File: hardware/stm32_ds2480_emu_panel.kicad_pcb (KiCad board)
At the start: 2 copper layers, 70 x 84 mm, 288 parts, among them J1 OW, J2 USB_A, J3 SWD, Q1 SI2302CDS, U1 USBLC6-2SC6, U2 STM32F042F6Px, U3 AP2204K-3.3

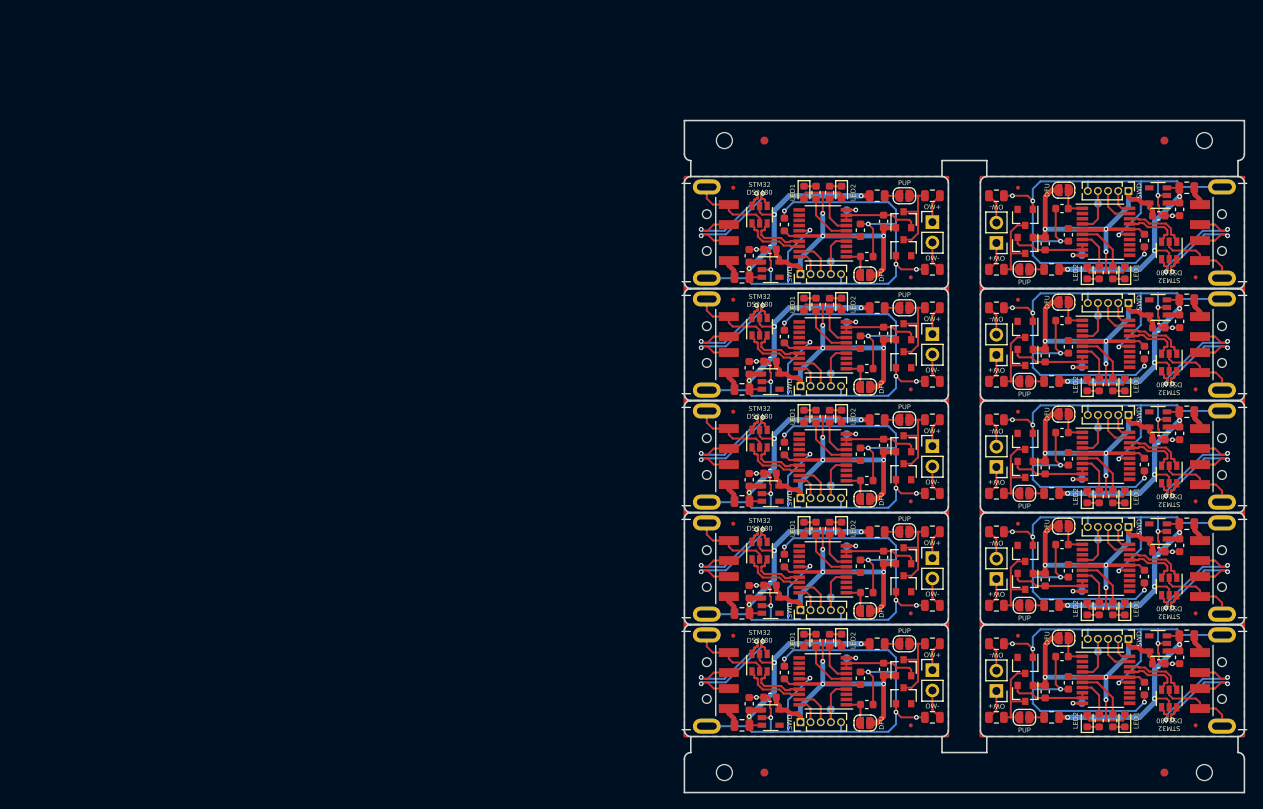
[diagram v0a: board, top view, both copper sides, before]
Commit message: Started using KiKit for the panelization.
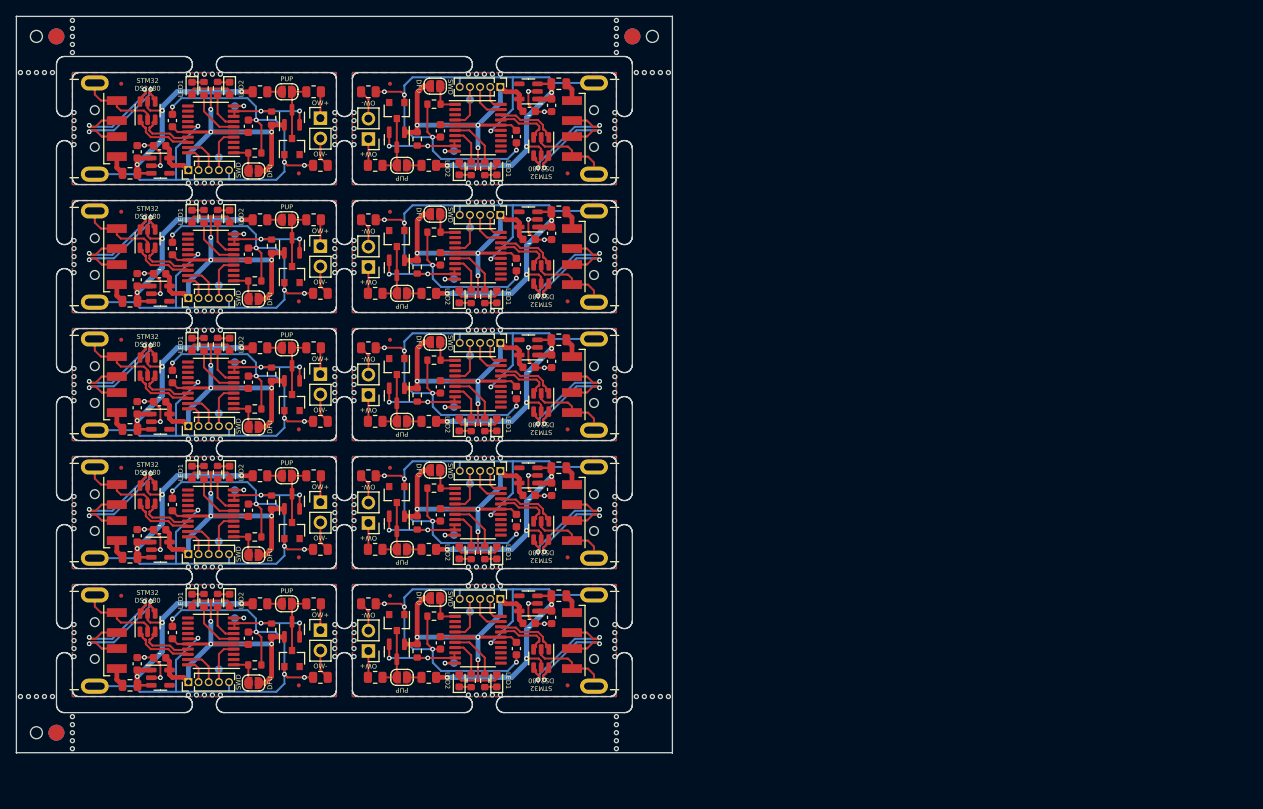
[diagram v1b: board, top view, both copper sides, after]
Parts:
- removed the C1 at (167.5, 120.0)
- removed the C1 at (122.5, 62.0)
- removed the C1 at (167.5, 106.0)
- removed the C1 at (167.5, 92.0)
- removed the C1 at (167.5, 78.0)
- removed the C1 at (122.5, 118.0)
- removed the C1 at (122.5, 104.0)
- removed the C1 at (122.5, 90.0)
- removed the C1 at (122.5, 76.0)
- removed the C1 at (167.5, 64.0)
- removed the C2 at (158.0, 119.3)
- removed the C2 at (132.0, 62.7)
- removed the C2 at (158.0, 105.3)
- removed the C2 at (158.0, 91.3)
- removed the C2 at (158.0, 77.3)
- removed the C2 at (132.0, 118.7)
- removed the C2 at (132.0, 104.7)
- removed the C2 at (132.0, 90.7)
- removed the C2 at (132.0, 76.7)
- removed the C2 at (158.0, 63.3)
- removed the C3 at (169.3, 116.9)
- removed the C3 at (120.7, 65.1)
- removed the C3 at (169.3, 102.9)
- removed the C3 at (169.3, 88.9)
- removed the C3 at (169.3, 74.9)
- removed the C3 at (120.7, 121.1)
- removed the C3 at (120.7, 107.1)
- removed the C3 at (120.7, 93.1)
- removed the C3 at (120.7, 79.1)
- removed the C3 at (169.3, 60.9)
- removed the C4 at (171.9, 116.1)
- removed the C4 at (118.1, 65.9)
- removed the C4 at (171.9, 102.1)
- removed the C4 at (171.9, 88.1)
- removed the C4 at (171.9, 74.1)
- removed the C4 at (118.1, 121.9)
- removed the C4 at (118.1, 107.9)
- removed the C4 at (118.1, 93.9)
- removed the C4 at (118.1, 79.9)
- removed the C4 at (171.9, 60.1)
- removed the D1 at (125.0, 114.0)
- removed the D1 at (125.0, 58.0)
- removed the D1 at (125.0, 100.0)
- removed the D1 at (125.0, 86.0)
- removed the D1 at (125.0, 72.0)
- removed the D1 at (165.1, 124.0)
- removed the D1 at (165.1, 110.0)
- removed the D1 at (165.1, 96.0)
- removed the D1 at (165.1, 82.0)
- removed the D1 at (165.1, 68.0)
- removed the D2 at (160.3, 124.0)
- removed the D2 at (129.7, 58.0)
- removed the D2 at (160.3, 110.0)
- removed the D2 at (160.3, 96.0)
- removed the D2 at (160.3, 82.0)
- removed the D2 at (129.7, 114.0)
- removed the D2 at (129.7, 100.0)
- removed the D2 at (129.7, 86.0)
- removed the D2 at (129.7, 72.0)
- removed the D2 at (160.3, 68.0)
- removed the D3 at (152.6, 117.1)
- removed the D3 at (137.4, 64.9)
- removed the D3 at (152.6, 103.1)
- removed the D3 at (152.6, 89.1)
- removed the D3 at (152.6, 75.1)
- removed the D3 at (137.4, 120.9)
- removed the D3 at (137.4, 106.9)
- removed the D3 at (137.4, 92.9)
- removed the D3 at (137.4, 78.9)
- removed the D3 at (152.6, 61.1)
- removed the F1 at (117.2, 124.6)
- removed the F1 at (117.2, 68.6)
- removed the F1 at (117.2, 110.6)
- removed the F1 at (117.2, 96.6)
- removed the F1 at (117.2, 82.6)
- removed the F1 at (172.8, 113.4)
- removed the F1 at (172.8, 99.4)
- removed the F1 at (172.8, 85.4)
- removed the F1 at (172.8, 71.4)
- removed the F1 at (172.8, 57.4)
- removed the FID1 at (173.9, 124.6)
- removed the FID1 at (116.1, 57.4)
- removed the FID1 at (173.9, 110.6)
- removed the FID1 at (173.9, 96.6)
- removed the FID1 at (173.9, 82.6)
- removed the FID1 at (116.1, 113.4)
- removed the FID1 at (116.1, 99.4)
- removed the FID1 at (116.1, 85.4)
- removed the FID1 at (116.1, 71.4)
- removed the FID1 at (173.9, 68.6)
- removed the FID2 at (138.3, 124.6)
- removed the FID2 at (138.3, 68.6)
- removed the FID2 at (138.3, 110.6)
- removed the FID2 at (138.3, 96.6)
- removed the FID2 at (138.3, 82.6)
- removed the FID2 at (151.7, 113.4)
- removed the FID2 at (151.7, 99.4)
- removed the FID2 at (151.7, 85.4)
- removed the FID2 at (151.7, 71.4)
- removed the FID2 at (151.7, 57.4)
- removed FID_A1 (x2), FID_A2 (x2): Fiducial_1mm_Mask2mm, Fiducial:Fiducial_1mm_Mask2mm
- removed the J1 at (141.0, 117.7)
- removed the J1 at (141.0, 61.7)
- removed the J1 at (141.0, 103.7)
- removed the J1 at (141.0, 89.7)
- removed the J1 at (141.0, 75.7)
- removed the J1 at (149.0, 120.3)
- removed the J1 at (149.0, 106.3)
- removed the J1 at (149.0, 92.3)
- removed the J1 at (149.0, 78.3)
- removed the J1 at (149.0, 64.3)
- removed the J2 at (105.9, 119.0)
- removed the J2 at (105.9, 63.0)
- removed the J2 at (105.9, 105.0)
- removed the J2 at (105.9, 91.0)
- removed the J2 at (105.9, 77.0)
- removed the J2 at (184.1, 119.0)
- removed the J2 at (184.1, 105.0)
- removed the J2 at (184.1, 91.0)
- removed the J2 at (184.1, 77.0)
- removed the J2 at (184.1, 63.0)
- removed the J3 at (165.5, 113.8)
- removed the J3 at (124.5, 68.2)
- removed the J3 at (165.5, 99.8)
- removed the J3 at (165.5, 85.8)
- removed the J3 at (165.5, 71.8)
- removed the J3 at (124.5, 124.2)
- removed the J3 at (124.5, 110.2)
- removed the J3 at (124.5, 96.2)
- removed the J3 at (124.5, 82.2)
- removed the J3 at (165.5, 57.8)
- removed the JP1 at (152.5, 123.6)
- removed the JP1 at (137.5, 58.4)
- removed the JP1 at (152.5, 109.6)
- removed the JP1 at (152.5, 95.6)
- removed the JP1 at (152.5, 81.6)
- removed the JP1 at (137.5, 114.4)
- removed the JP1 at (137.5, 100.4)
- removed the JP1 at (137.5, 86.4)
- removed the JP1 at (137.5, 72.4)
- removed the JP1 at (152.5, 67.6)
- removed the JP2 at (132.6, 124.3)
- removed the JP2 at (132.6, 68.3)
- removed the JP2 at (132.6, 110.3)
- removed the JP2 at (132.6, 96.3)
- removed the JP2 at (132.6, 82.3)
- removed the JP2 at (157.4, 113.7)
- removed the JP2 at (157.4, 99.7)
- removed the JP2 at (157.4, 85.7)
- removed the JP2 at (157.4, 71.7)
- removed the JP2 at (157.4, 57.7)
- removed the Q1 at (152.6, 120.6)
- removed the Q1 at (137.4, 61.4)
- removed the Q1 at (152.6, 106.6)
- removed the Q1 at (152.6, 92.6)
- removed the Q1 at (152.6, 78.6)
- removed the Q1 at (137.4, 117.4)
- removed the Q1 at (137.4, 103.4)
- removed the Q1 at (137.4, 89.4)
- removed the Q1 at (137.4, 75.4)
- removed the Q1 at (152.6, 64.6)
- removed the R1 at (163.6, 124.0)
- removed the R1 at (126.5, 58.0)
- removed the R1 at (163.6, 110.0)
- removed the R1 at (163.6, 96.0)
- removed the R1 at (163.6, 82.0)
- removed the R1 at (126.5, 114.0)
- removed the R1 at (126.5, 100.0)
- removed the R1 at (126.5, 86.0)
- removed the R1 at (126.5, 72.0)
- removed the R1 at (163.6, 68.0)
- removed the R2 at (161.8, 124.0)
- removed the R2 at (128.2, 58.0)
- removed the R2 at (161.8, 110.0)
- removed the R2 at (161.8, 96.0)
- removed the R2 at (161.8, 82.0)
- removed the R2 at (128.2, 114.0)
- removed the R2 at (128.2, 100.0)
- removed the R2 at (128.2, 86.0)
- removed the R2 at (128.2, 72.0)
- removed the R2 at (161.8, 68.0)
- removed the R3 at (134.1, 114.4)
- removed the R3 at (134.1, 58.4)
- removed the R3 at (134.1, 100.4)
- removed the R3 at (134.1, 86.4)
- removed the R3 at (134.1, 72.4)
- removed the R3 at (155.9, 123.6)
- removed the R3 at (155.9, 109.6)
- removed the R3 at (155.9, 95.6)
- removed the R3 at (155.9, 81.6)
- removed the R3 at (155.9, 67.6)
- removed the R4 at (141.0, 114.4)
- removed the R4 at (141.0, 58.4)
- removed the R4 at (141.0, 100.4)
- removed the R4 at (141.0, 86.4)
- removed the R4 at (141.0, 72.4)
- removed the R4 at (149.0, 123.6)
- removed the R4 at (149.0, 109.6)
- removed the R4 at (149.0, 95.6)
- removed the R4 at (149.0, 81.6)
- removed the R4 at (149.0, 67.6)
- removed the R5 at (155.1, 120.4)
- removed the R5 at (134.9, 61.6)
- removed the R5 at (155.1, 106.4)
- removed the R5 at (155.1, 92.4)
- removed the R5 at (155.1, 78.4)
- removed the R5 at (134.9, 117.6)
- removed the R5 at (134.9, 103.6)
- removed the R5 at (134.9, 89.6)
- removed the R5 at (134.9, 75.6)
- removed the R5 at (155.1, 64.4)
- removed the R6 at (157.2, 116.0)
- removed the R6 at (132.8, 66.0)
- removed the R6 at (157.2, 102.0)
- removed the R6 at (157.2, 88.0)
- removed the R6 at (157.2, 74.0)
- removed the R6 at (132.8, 122.0)
- removed the R6 at (132.8, 108.0)
- removed the R6 at (132.8, 94.0)
- removed the R6 at (132.8, 80.0)
- removed the R6 at (157.2, 60.0)
- removed the R7 at (149.0, 114.4)
- removed the R7 at (141.0, 67.6)
- removed the R7 at (149.0, 100.4)
- removed the R7 at (149.0, 86.4)
- removed the R7 at (149.0, 72.4)
- removed the R7 at (141.0, 123.6)
- removed the R7 at (141.0, 109.6)
- removed the R7 at (141.0, 95.6)
- removed the R7 at (141.0, 81.6)
- removed the R7 at (149.0, 58.4)
- removed the REF** at (115.0, 130.5)
- removed the REF** at (175.0, 130.5)
- removed the REF** at (115.0, 51.5)
- removed the REF** at (175.0, 51.5)
- removed the TP1 at (159.7, 121.8)
- removed the TP1 at (130.3, 60.2)
- removed the TP1 at (159.7, 107.8)
- removed the TP1 at (159.7, 93.8)
- removed the TP1 at (159.7, 79.8)
- removed the TP1 at (130.3, 116.2)
- removed the TP1 at (130.3, 102.2)
- removed the TP1 at (130.3, 88.2)
- removed the TP1 at (130.3, 74.2)
- removed the TP1 at (159.7, 65.8)
- removed the TP2 at (161.7, 115.4)
- removed the TP2 at (128.3, 66.6)
- removed the TP2 at (161.7, 101.4)
- removed the TP2 at (161.7, 87.4)
- removed the TP2 at (161.7, 73.4)
- removed the TP2 at (128.3, 122.6)
- removed the TP2 at (128.3, 108.6)
- removed the TP2 at (128.3, 94.6)
- removed the TP2 at (128.3, 80.6)
- removed the TP2 at (161.7, 59.4)
- removed the U1 at (170.6, 121.2)
- removed the U1 at (119.4, 60.8)
- removed the U1 at (170.6, 107.2)
- removed the U1 at (170.6, 93.2)
- removed the U1 at (170.6, 79.2)
- removed the U1 at (119.4, 116.8)
- removed the U1 at (119.4, 102.8)
- removed the U1 at (119.4, 88.8)
- removed the U1 at (119.4, 74.8)
- removed the U1 at (170.6, 65.2)
- removed the U2 at (162.7, 118.9)
- removed the U2 at (127.3, 63.1)
- removed the U2 at (162.7, 104.9)
- removed the U2 at (162.7, 90.9)
- removed the U2 at (162.7, 76.9)
- removed the U2 at (127.3, 119.1)
- removed the U2 at (127.3, 105.1)
- removed the U2 at (127.3, 91.1)
- removed the U2 at (127.3, 77.1)
- removed the U2 at (162.7, 62.9)
- removed the U3 at (169.2, 114.4)
- removed the U3 at (120.8, 67.6)
- removed the U3 at (169.2, 100.4)
- removed the U3 at (169.2, 86.4)
- removed the U3 at (169.2, 72.4)
- removed the U3 at (120.8, 123.6)
- removed the U3 at (120.8, 109.6)
- removed the U3 at (120.8, 95.6)
- removed the U3 at (120.8, 81.6)
- removed the U3 at (169.2, 58.4)
- added C1: 100nF, Capacitor_SMD:C_0603_1608Metric, F.Cu at (89.0, 99.0)
- added C1: 100nF, Capacitor_SMD:C_0603_1608Metric, F.Cu at (46.0, 65.0)
- added C1: 100nF, Capacitor_SMD:C_0603_1608Metric, F.Cu at (89.0, 67.0)
- added C1: 100nF, Capacitor_SMD:C_0603_1608Metric, F.Cu at (46.0, 97.0)
- added C1: 100nF, Capacitor_SMD:C_0603_1608Metric, F.Cu at (46.0, 81.0)
- added C1: 100nF, Capacitor_SMD:C_0603_1608Metric, F.Cu at (89.0, 51.0)
- added C1: 100nF, Capacitor_SMD:C_0603_1608Metric, F.Cu at (46.0, 49.0)
- added C1: 100nF, Capacitor_SMD:C_0603_1608Metric, F.Cu at (46.0, 113.0)
- added C1: 100nF, Capacitor_SMD:C_0603_1608Metric, F.Cu at (89.0, 83.0)
- added C1: 100nF, Capacitor_SMD:C_0603_1608Metric, F.Cu at (89.0, 115.0)
- added C2: 100nF, Capacitor_SMD:C_0603_1608Metric, F.Cu at (55.5, 81.7)
- added C2: 100nF, Capacitor_SMD:C_0603_1608Metric, F.Cu at (55.5, 113.7)
- added C2: 100nF, Capacitor_SMD:C_0603_1608Metric, F.Cu at (55.5, 65.7)
- added C2: 100nF, Capacitor_SMD:C_0603_1608Metric, F.Cu at (79.5, 114.3)
- added C2: 100nF, Capacitor_SMD:C_0603_1608Metric, F.Cu at (79.5, 98.3)
- added C2: 100nF, Capacitor_SMD:C_0603_1608Metric, F.Cu at (79.5, 82.3)
- added C2: 100nF, Capacitor_SMD:C_0603_1608Metric, F.Cu at (55.5, 97.7)
- added C2: 100nF, Capacitor_SMD:C_0603_1608Metric, F.Cu at (79.5, 50.3)
- added C2: 100nF, Capacitor_SMD:C_0603_1608Metric, F.Cu at (79.5, 66.3)
- added C2: 100nF, Capacitor_SMD:C_0603_1608Metric, F.Cu at (55.5, 49.7)
- added C3: 2.2uF, Capacitor_SMD:C_0603_1608Metric, F.Cu at (90.6, 79.9)
- added C3: 2.2uF, Capacitor_SMD:C_0603_1608Metric, F.Cu at (44.4, 52.1)
- added C3: 2.2uF, Capacitor_SMD:C_0603_1608Metric, F.Cu at (44.4, 116.2)
- added C3: 2.2uF, Capacitor_SMD:C_0603_1608Metric, F.Cu at (44.4, 68.2)
- added C3: 2.2uF, Capacitor_SMD:C_0603_1608Metric, F.Cu at (90.6, 63.9)
- added C3: 2.2uF, Capacitor_SMD:C_0603_1608Metric, F.Cu at (90.6, 47.9)
- added C3: 2.2uF, Capacitor_SMD:C_0603_1608Metric, F.Cu at (44.4, 100.2)
- added C3: 2.2uF, Capacitor_SMD:C_0603_1608Metric, F.Cu at (90.6, 95.9)
- added C3: 2.2uF, Capacitor_SMD:C_0603_1608Metric, F.Cu at (44.4, 84.2)
- added C3: 2.2uF, Capacitor_SMD:C_0603_1608Metric, F.Cu at (90.6, 111.9)
- added C4: 1uF, Capacitor_SMD:C_0603_1608Metric, F.Cu at (41.6, 116.9)
- added C4: 1uF, Capacitor_SMD:C_0603_1608Metric, F.Cu at (41.6, 52.9)
- added C4: 1uF, Capacitor_SMD:C_0603_1608Metric, F.Cu at (93.4, 95.1)
- added C4: 1uF, Capacitor_SMD:C_0603_1608Metric, F.Cu at (93.4, 63.1)
- added C4: 1uF, Capacitor_SMD:C_0603_1608Metric, F.Cu at (93.4, 47.1)
- added C4: 1uF, Capacitor_SMD:C_0603_1608Metric, F.Cu at (41.6, 100.9)
- added C4: 1uF, Capacitor_SMD:C_0603_1608Metric, F.Cu at (41.6, 68.9)
- added C4: 1uF, Capacitor_SMD:C_0603_1608Metric, F.Cu at (41.6, 84.9)
- added C4: 1uF, Capacitor_SMD:C_0603_1608Metric, F.Cu at (93.4, 111.1)
- added C4: 1uF, Capacitor_SMD:C_0603_1608Metric, F.Cu at (93.4, 79.1)
- added D1: LED1, LED_SMD:LED_0603_1608Metric, F.Cu at (86.6, 119.0)
- added D1: LED1, LED_SMD:LED_0603_1608Metric, F.Cu at (48.4, 93.0)
- added D1: LED1, LED_SMD:LED_0603_1608Metric, F.Cu at (86.6, 71.0)
- added D1: LED1, LED_SMD:LED_0603_1608Metric, F.Cu at (48.4, 77.0)
- added D1: LED1, LED_SMD:LED_0603_1608Metric, F.Cu at (86.6, 87.0)
- added D1: LED1, LED_SMD:LED_0603_1608Metric, F.Cu at (48.4, 45.0)
- added D1: LED1, LED_SMD:LED_0603_1608Metric, F.Cu at (48.4, 61.0)
- added D1: LED1, LED_SMD:LED_0603_1608Metric, F.Cu at (86.6, 103.0)
- added D1: LED1, LED_SMD:LED_0603_1608Metric, F.Cu at (48.4, 109.0)
- added D1: LED1, LED_SMD:LED_0603_1608Metric, F.Cu at (86.6, 55.0)
- added D2: LED2, LED_SMD:LED_0603_1608Metric, F.Cu at (81.9, 103.0)
- added D2: LED2, LED_SMD:LED_0603_1608Metric, F.Cu at (81.9, 87.0)
- added D2: LED2, LED_SMD:LED_0603_1608Metric, F.Cu at (53.1, 61.0)
- added D2: LED2, LED_SMD:LED_0603_1608Metric, F.Cu at (81.9, 119.0)
- added D2: LED2, LED_SMD:LED_0603_1608Metric, F.Cu at (53.1, 77.0)
- added D2: LED2, LED_SMD:LED_0603_1608Metric, F.Cu at (81.9, 55.0)
- added D2: LED2, LED_SMD:LED_0603_1608Metric, F.Cu at (53.1, 109.0)
- added D2: LED2, LED_SMD:LED_0603_1608Metric, F.Cu at (53.1, 93.0)
- added D2: LED2, LED_SMD:LED_0603_1608Metric, F.Cu at (53.1, 45.0)
- added D2: LED2, LED_SMD:LED_0603_1608Metric, F.Cu at (81.9, 71.0)
- added D3: 5.1V, Diode_SMD:D_SOT-23_ANK, F.Cu at (60.9, 84.3)
- added D3: 5.1V, Diode_SMD:D_SOT-23_ANK, F.Cu at (74.1, 95.8)
- added D3: 5.1V, Diode_SMD:D_SOT-23_ANK, F.Cu at (74.1, 63.8)
- added D3: 5.1V, Diode_SMD:D_SOT-23_ANK, F.Cu at (60.9, 68.3)
- added D3: 5.1V, Diode_SMD:D_SOT-23_ANK, F.Cu at (74.1, 79.8)
- added D3: 5.1V, Diode_SMD:D_SOT-23_ANK, F.Cu at (74.1, 47.8)
- added D3: 5.1V, Diode_SMD:D_SOT-23_ANK, F.Cu at (60.9, 52.2)
- added D3: 5.1V, Diode_SMD:D_SOT-23_ANK, F.Cu at (74.1, 111.8)
- added D3: 5.1V, Diode_SMD:D_SOT-23_ANK, F.Cu at (60.9, 100.3)
- added D3: 5.1V, Diode_SMD:D_SOT-23_ANK, F.Cu at (60.9, 116.3)
- added F1: Polyfuse, Fuse:Fuse_0805_2012Metric, F.Cu at (94.3, 60.4)
- added F1: Polyfuse, Fuse:Fuse_0805_2012Metric, F.Cu at (40.7, 55.6)
- added F1: Polyfuse, Fuse:Fuse_0805_2012Metric, F.Cu at (94.3, 92.4)
- added F1: Polyfuse, Fuse:Fuse_0805_2012Metric, F.Cu at (40.7, 87.6)
- added F1: Polyfuse, Fuse:Fuse_0805_2012Metric, F.Cu at (40.7, 103.6)
- added F1: Polyfuse, Fuse:Fuse_0805_2012Metric, F.Cu at (94.3, 108.4)
- added F1: Polyfuse, Fuse:Fuse_0805_2012Metric, F.Cu at (94.3, 44.4)
- added F1: Polyfuse, Fuse:Fuse_0805_2012Metric, F.Cu at (94.3, 76.4)
- added F1: Polyfuse, Fuse:Fuse_0805_2012Metric, F.Cu at (40.7, 119.6)
- added F1: Polyfuse, Fuse:Fuse_0805_2012Metric, F.Cu at (40.7, 71.6)
- added FID1: Fiducial, Fiducial:Fiducial_0.5mm_Mask1.5mm, F.Cu at (39.6, 108.4)
- added FID1: Fiducial, Fiducial:Fiducial_0.5mm_Mask1.5mm, F.Cu at (39.6, 60.4)
- added FID1: Fiducial, Fiducial:Fiducial_0.5mm_Mask1.5mm, F.Cu at (95.4, 103.6)
- added FID1: Fiducial, Fiducial:Fiducial_0.5mm_Mask1.5mm, F.Cu at (39.6, 92.4)
- added FID1: Fiducial, Fiducial:Fiducial_0.5mm_Mask1.5mm, F.Cu at (39.6, 44.4)
- added FID1: Fiducial, Fiducial:Fiducial_0.5mm_Mask1.5mm, F.Cu at (39.6, 76.4)
- added FID1: Fiducial, Fiducial:Fiducial_0.5mm_Mask1.5mm, F.Cu at (95.4, 71.6)
- added FID1: Fiducial, Fiducial:Fiducial_0.5mm_Mask1.5mm, F.Cu at (95.4, 55.6)
- added FID1: Fiducial, Fiducial:Fiducial_0.5mm_Mask1.5mm, F.Cu at (95.4, 87.6)
- added FID1: Fiducial, Fiducial:Fiducial_0.5mm_Mask1.5mm, F.Cu at (95.4, 119.6)
- added FID2: Fiducial, Fiducial:Fiducial_0.5mm_Mask1.5mm, F.Cu at (73.2, 44.4)
- added FID2: Fiducial, Fiducial:Fiducial_0.5mm_Mask1.5mm, F.Cu at (73.2, 60.4)
- added FID2: Fiducial, Fiducial:Fiducial_0.5mm_Mask1.5mm, F.Cu at (73.2, 92.4)
- added FID2: Fiducial, Fiducial:Fiducial_0.5mm_Mask1.5mm, F.Cu at (61.8, 55.6)
- added FID2: Fiducial, Fiducial:Fiducial_0.5mm_Mask1.5mm, F.Cu at (61.8, 103.6)
- added FID2: Fiducial, Fiducial:Fiducial_0.5mm_Mask1.5mm, F.Cu at (61.8, 87.6)
- added FID2: Fiducial, Fiducial:Fiducial_0.5mm_Mask1.5mm, F.Cu at (61.8, 119.6)
- added FID2: Fiducial, Fiducial:Fiducial_0.5mm_Mask1.5mm, F.Cu at (73.2, 108.4)
- added FID2: Fiducial, Fiducial:Fiducial_0.5mm_Mask1.5mm, F.Cu at (73.2, 76.4)
- added FID2: Fiducial, Fiducial:Fiducial_0.5mm_Mask1.5mm, F.Cu at (61.8, 71.6)
- added J1: OW, Connector_PinHeader_2.54mm:PinHeader_1x02_P2.54mm_Vertical, F.Cu at (70.5, 83.3)
- added J1: OW, Connector_PinHeader_2.54mm:PinHeader_1x02_P2.54mm_Vertical, F.Cu at (64.5, 48.7)
- added J1: OW, Connector_PinHeader_2.54mm:PinHeader_1x02_P2.54mm_Vertical, F.Cu at (64.5, 112.7)
- added J1: OW, Connector_PinHeader_2.54mm:PinHeader_1x02_P2.54mm_Vertical, F.Cu at (70.5, 115.3)
- added J1: OW, Connector_PinHeader_2.54mm:PinHeader_1x02_P2.54mm_Vertical, F.Cu at (64.5, 64.7)
- added J1: OW, Connector_PinHeader_2.54mm:PinHeader_1x02_P2.54mm_Vertical, F.Cu at (70.5, 99.3)
- added J1: OW, Connector_PinHeader_2.54mm:PinHeader_1x02_P2.54mm_Vertical, F.Cu at (64.5, 80.7)
- added J1: OW, Connector_PinHeader_2.54mm:PinHeader_1x02_P2.54mm_Vertical, F.Cu at (70.5, 67.3)
- added J1: OW, Connector_PinHeader_2.54mm:PinHeader_1x02_P2.54mm_Vertical, F.Cu at (64.5, 96.7)
- added J1: OW, Connector_PinHeader_2.54mm:PinHeader_1x02_P2.54mm_Vertical, F.Cu at (70.5, 51.3)
- added J2: USB_A, Connector_USB:USB_A_CNCTech_1001-011-01101_Horizontal, F.Cu at (105.6, 50.0)
- added J2: USB_A, Connector_USB:USB_A_CNCTech_1001-011-01101_Horizontal, F.Cu at (29.4, 114.0)
- added J2: USB_A, Connector_USB:USB_A_CNCTech_1001-011-01101_Horizontal, F.Cu at (105.6, 66.0)
- added J2: USB_A, Connector_USB:USB_A_CNCTech_1001-011-01101_Horizontal, F.Cu at (29.4, 82.0)
- added J2: USB_A, Connector_USB:USB_A_CNCTech_1001-011-01101_Horizontal, F.Cu at (105.6, 82.0)
- added J2: USB_A, Connector_USB:USB_A_CNCTech_1001-011-01101_Horizontal, F.Cu at (105.6, 98.0)
- added J2: USB_A, Connector_USB:USB_A_CNCTech_1001-011-01101_Horizontal, F.Cu at (29.4, 98.0)
- added J2: USB_A, Connector_USB:USB_A_CNCTech_1001-011-01101_Horizontal, F.Cu at (29.4, 50.0)
- added J2: USB_A, Connector_USB:USB_A_CNCTech_1001-011-01101_Horizontal, F.Cu at (105.6, 114.0)
- added J2: USB_A, Connector_USB:USB_A_CNCTech_1001-011-01101_Horizontal, F.Cu at (29.4, 66.0)
- added J3: SWD, Connector_PinHeader_1.27mm:PinHeader_1x05_P1.27mm_Vertical, F.Cu at (48.0, 119.2)
- added J3: SWD, Connector_PinHeader_1.27mm:PinHeader_1x05_P1.27mm_Vertical, F.Cu at (87.0, 76.8)
- added J3: SWD, Connector_PinHeader_1.27mm:PinHeader_1x05_P1.27mm_Vertical, F.Cu at (87.0, 108.8)
- added J3: SWD, Connector_PinHeader_1.27mm:PinHeader_1x05_P1.27mm_Vertical, F.Cu at (48.0, 87.2)
- added J3: SWD, Connector_PinHeader_1.27mm:PinHeader_1x05_P1.27mm_Vertical, F.Cu at (87.0, 44.8)
- added J3: SWD, Connector_PinHeader_1.27mm:PinHeader_1x05_P1.27mm_Vertical, F.Cu at (87.0, 92.8)
- added J3: SWD, Connector_PinHeader_1.27mm:PinHeader_1x05_P1.27mm_Vertical, F.Cu at (48.0, 103.2)
- added J3: SWD, Connector_PinHeader_1.27mm:PinHeader_1x05_P1.27mm_Vertical, F.Cu at (87.0, 60.8)
- added J3: SWD, Connector_PinHeader_1.27mm:PinHeader_1x05_P1.27mm_Vertical, F.Cu at (48.0, 71.2)
- added J3: SWD, Connector_PinHeader_1.27mm:PinHeader_1x05_P1.27mm_Vertical, F.Cu at (48.0, 55.2)
- added JP1: PUP, Jumper:SolderJumper-2_P1.3mm_Open_RoundedPad1.0x1.5mm, F.Cu at (60.3, 61.4)
- added JP1: PUP, Jumper:SolderJumper-2_P1.3mm_Open_RoundedPad1.0x1.5mm, F.Cu at (74.7, 118.6)
- added JP1: PUP, Jumper:SolderJumper-2_P1.3mm_Open_RoundedPad1.0x1.5mm, F.Cu at (60.3, 77.4)
- added JP1: PUP, Jumper:SolderJumper-2_P1.3mm_Open_RoundedPad1.0x1.5mm, F.Cu at (74.7, 102.6)
- added JP1: PUP, Jumper:SolderJumper-2_P1.3mm_Open_RoundedPad1.0x1.5mm, F.Cu at (60.3, 45.4)
- added JP1: PUP, Jumper:SolderJumper-2_P1.3mm_Open_RoundedPad1.0x1.5mm, F.Cu at (74.7, 54.6)
- added JP1: PUP, Jumper:SolderJumper-2_P1.3mm_Open_RoundedPad1.0x1.5mm, F.Cu at (74.7, 86.6)
- added JP1: PUP, Jumper:SolderJumper-2_P1.3mm_Open_RoundedPad1.0x1.5mm, F.Cu at (60.3, 109.4)
- added JP1: PUP, Jumper:SolderJumper-2_P1.3mm_Open_RoundedPad1.0x1.5mm, F.Cu at (60.3, 93.4)
- added JP1: PUP, Jumper:SolderJumper-2_P1.3mm_Open_RoundedPad1.0x1.5mm, F.Cu at (74.7, 70.6)
- added JP2: DFU, Jumper:SolderJumper-2_P1.3mm_Open_RoundedPad1.0x1.5mm, F.Cu at (56.1, 71.3)
- added JP2: DFU, Jumper:SolderJumper-2_P1.3mm_Open_RoundedPad1.0x1.5mm, F.Cu at (56.1, 119.3)
- added JP2: DFU, Jumper:SolderJumper-2_P1.3mm_Open_RoundedPad1.0x1.5mm, F.Cu at (78.9, 60.7)
- added JP2: DFU, Jumper:SolderJumper-2_P1.3mm_Open_RoundedPad1.0x1.5mm, F.Cu at (78.9, 44.7)
- added JP2: DFU, Jumper:SolderJumper-2_P1.3mm_Open_RoundedPad1.0x1.5mm, F.Cu at (56.1, 55.3)
- added JP2: DFU, Jumper:SolderJumper-2_P1.3mm_Open_RoundedPad1.0x1.5mm, F.Cu at (78.9, 76.7)
- added JP2: DFU, Jumper:SolderJumper-2_P1.3mm_Open_RoundedPad1.0x1.5mm, F.Cu at (56.1, 103.3)
- added JP2: DFU, Jumper:SolderJumper-2_P1.3mm_Open_RoundedPad1.0x1.5mm, F.Cu at (78.9, 92.7)
- added JP2: DFU, Jumper:SolderJumper-2_P1.3mm_Open_RoundedPad1.0x1.5mm, F.Cu at (56.1, 87.3)
- added JP2: DFU, Jumper:SolderJumper-2_P1.3mm_Open_RoundedPad1.0x1.5mm, F.Cu at (78.9, 108.7)
- added Q1: SI2302CDS, Package_TO_SOT_SMD:SOT-23, F.Cu at (60.9, 80.6)
- added Q1: SI2302CDS, Package_TO_SOT_SMD:SOT-23, F.Cu at (60.9, 48.6)
- added Q1: SI2302CDS, Package_TO_SOT_SMD:SOT-23, F.Cu at (74.1, 67.4)
- added Q1: SI2302CDS, Package_TO_SOT_SMD:SOT-23, F.Cu at (60.9, 64.6)
- added Q1: SI2302CDS, Package_TO_SOT_SMD:SOT-23, F.Cu at (60.9, 112.6)
- added Q1: SI2302CDS, Package_TO_SOT_SMD:SOT-23, F.Cu at (60.9, 96.6)
- added Q1: SI2302CDS, Package_TO_SOT_SMD:SOT-23, F.Cu at (74.1, 99.4)
- added Q1: SI2302CDS, Package_TO_SOT_SMD:SOT-23, F.Cu at (74.1, 115.4)
- added Q1: SI2302CDS, Package_TO_SOT_SMD:SOT-23, F.Cu at (74.1, 51.4)
- added Q1: SI2302CDS, Package_TO_SOT_SMD:SOT-23, F.Cu at (74.1, 83.4)
- added R1: 100R, Resistor_SMD:R_0603_1608Metric, F.Cu at (49.9, 93.0)
- added R1: 100R, Resistor_SMD:R_0603_1608Metric, F.Cu at (85.1, 87.0)
- added R1: 100R, Resistor_SMD:R_0603_1608Metric, F.Cu at (85.1, 71.0)
- added R1: 100R, Resistor_SMD:R_0603_1608Metric, F.Cu at (49.9, 45.0)
- added R1: 100R, Resistor_SMD:R_0603_1608Metric, F.Cu at (49.9, 61.0)
- added R1: 100R, Resistor_SMD:R_0603_1608Metric, F.Cu at (85.1, 55.0)
- added R1: 100R, Resistor_SMD:R_0603_1608Metric, F.Cu at (49.9, 109.0)
- added R1: 100R, Resistor_SMD:R_0603_1608Metric, F.Cu at (85.1, 103.0)
- added R1: 100R, Resistor_SMD:R_0603_1608Metric, F.Cu at (85.1, 119.0)
- added R1: 100R, Resistor_SMD:R_0603_1608Metric, F.Cu at (49.9, 77.0)
- added R2: 100R, Resistor_SMD:R_0603_1608Metric, F.Cu at (51.6, 45.0)
- added R2: 100R, Resistor_SMD:R_0603_1608Metric, F.Cu at (83.4, 103.0)
- added R2: 100R, Resistor_SMD:R_0603_1608Metric, F.Cu at (51.6, 109.0)
- added R2: 100R, Resistor_SMD:R_0603_1608Metric, F.Cu at (83.4, 71.0)
- added R2: 100R, Resistor_SMD:R_0603_1608Metric, F.Cu at (51.6, 61.0)
- added R2: 100R, Resistor_SMD:R_0603_1608Metric, F.Cu at (83.4, 87.0)
- added R2: 100R, Resistor_SMD:R_0603_1608Metric, F.Cu at (83.4, 119.0)
- added R2: 100R, Resistor_SMD:R_0603_1608Metric, F.Cu at (83.4, 55.0)
- added R2: 100R, Resistor_SMD:R_0603_1608Metric, F.Cu at (51.6, 77.0)
- added R2: 100R, Resistor_SMD:R_0603_1608Metric, F.Cu at (51.6, 93.0)
- added R3: 2.2K, Resistor_SMD:R_0805_2012Metric, F.Cu at (56.9, 77.4)
- added R3: 2.2K, Resistor_SMD:R_0805_2012Metric, F.Cu at (78.1, 54.6)
- added R3: 2.2K, Resistor_SMD:R_0805_2012Metric, F.Cu at (78.1, 118.6)
- added R3: 2.2K, Resistor_SMD:R_0805_2012Metric, F.Cu at (56.9, 109.4)
- added R3: 2.2K, Resistor_SMD:R_0805_2012Metric, F.Cu at (56.9, 45.4)
- added R3: 2.2K, Resistor_SMD:R_0805_2012Metric, F.Cu at (56.9, 61.4)
- added R3: 2.2K, Resistor_SMD:R_0805_2012Metric, F.Cu at (78.1, 86.6)
- added R3: 2.2K, Resistor_SMD:R_0805_2012Metric, F.Cu at (78.1, 102.6)
- added R3: 2.2K, Resistor_SMD:R_0805_2012Metric, F.Cu at (56.9, 93.4)
- added R3: 2.2K, Resistor_SMD:R_0805_2012Metric, F.Cu at (78.1, 70.6)
- added R4: 4.7R, Resistor_SMD:R_0805_2012Metric, F.Cu at (71.4, 54.6)
- added R4: 4.7R, Resistor_SMD:R_0805_2012Metric, F.Cu at (71.4, 86.6)
- added R4: 4.7R, Resistor_SMD:R_0805_2012Metric, F.Cu at (63.6, 109.4)
- added R4: 4.7R, Resistor_SMD:R_0805_2012Metric, F.Cu at (71.4, 70.6)
- added R4: 4.7R, Resistor_SMD:R_0805_2012Metric, F.Cu at (63.6, 77.4)
- added R4: 4.7R, Resistor_SMD:R_0805_2012Metric, F.Cu at (63.6, 93.4)
- added R4: 4.7R, Resistor_SMD:R_0805_2012Metric, F.Cu at (63.6, 45.4)
- added R4: 4.7R, Resistor_SMD:R_0805_2012Metric, F.Cu at (71.4, 118.6)
- added R4: 4.7R, Resistor_SMD:R_0805_2012Metric, F.Cu at (71.4, 102.6)
- added R4: 4.7R, Resistor_SMD:R_0805_2012Metric, F.Cu at (63.6, 61.4)
- added R5: 10K, Resistor_SMD:R_0603_1608Metric, F.Cu at (76.6, 51.3)
- added R5: 10K, Resistor_SMD:R_0603_1608Metric, F.Cu at (58.4, 96.7)
- added R5: 10K, Resistor_SMD:R_0603_1608Metric, F.Cu at (58.4, 48.7)
- added R5: 10K, Resistor_SMD:R_0603_1608Metric, F.Cu at (76.6, 67.3)
- added R5: 10K, Resistor_SMD:R_0603_1608Metric, F.Cu at (58.4, 64.7)
- added R5: 10K, Resistor_SMD:R_0603_1608Metric, F.Cu at (76.6, 115.3)
- added R5: 10K, Resistor_SMD:R_0603_1608Metric, F.Cu at (76.6, 83.3)
- added R5: 10K, Resistor_SMD:R_0603_1608Metric, F.Cu at (58.4, 112.7)
- added R5: 10K, Resistor_SMD:R_0603_1608Metric, F.Cu at (58.4, 80.7)
- added R5: 10K, Resistor_SMD:R_0603_1608Metric, F.Cu at (76.6, 99.3)
- added R6: 10K, Resistor_SMD:R_0603_1608Metric, F.Cu at (78.7, 95.0)
- added R6: 10K, Resistor_SMD:R_0603_1608Metric, F.Cu at (56.3, 69.1)
- added R6: 10K, Resistor_SMD:R_0603_1608Metric, F.Cu at (78.7, 47.0)
- added R6: 10K, Resistor_SMD:R_0603_1608Metric, F.Cu at (56.3, 117.1)
- added R6: 10K, Resistor_SMD:R_0603_1608Metric, F.Cu at (56.3, 85.1)
- added R6: 10K, Resistor_SMD:R_0603_1608Metric, F.Cu at (78.7, 63.0)
- added R6: 10K, Resistor_SMD:R_0603_1608Metric, F.Cu at (56.3, 53.0)
- added R6: 10K, Resistor_SMD:R_0603_1608Metric, F.Cu at (78.7, 79.0)
- added R6: 10K, Resistor_SMD:R_0603_1608Metric, F.Cu at (78.7, 111.0)
- added R6: 10K, Resistor_SMD:R_0603_1608Metric, F.Cu at (56.3, 101.1)
- added R7: 4.7R, Resistor_SMD:R_0805_2012Metric, F.Cu at (64.5, 54.6)
- added R7: 4.7R, Resistor_SMD:R_0805_2012Metric, F.Cu at (64.5, 118.6)
- added R7: 4.7R, Resistor_SMD:R_0805_2012Metric, F.Cu at (70.5, 93.4)
- added R7: 4.7R, Resistor_SMD:R_0805_2012Metric, F.Cu at (64.5, 86.6)
- added R7: 4.7R, Resistor_SMD:R_0805_2012Metric, F.Cu at (64.5, 102.6)
- added R7: 4.7R, Resistor_SMD:R_0805_2012Metric, F.Cu at (70.5, 77.4)
- added R7: 4.7R, Resistor_SMD:R_0805_2012Metric, F.Cu at (64.5, 70.6)
- added R7: 4.7R, Resistor_SMD:R_0805_2012Metric, F.Cu at (70.5, 45.4)
- added R7: 4.7R, Resistor_SMD:R_0805_2012Metric, F.Cu at (70.5, 109.4)
- added R7: 4.7R, Resistor_SMD:R_0805_2012Metric, F.Cu at (70.5, 61.4)
- added REF**: NPTH, NPTH, F.Cu at (33.7, 100.0)
- added REF**: NPTH, NPTH, F.Cu at (86.0, 75.2)
- added REF**: NPTH, NPTH, F.Cu at (107.0, 121.0)
- added REF**: NPTH, NPTH, F.Cu at (33.7, 50.0)
- added REF**: NPTH, NPTH, F.Cu at (86.0, 91.2)
- added REF**: NPTH, NPTH, F.Cu at (101.3, 51.0)
- added REF**: NPTH, NPTH, F.Cu at (68.7, 98.0)
- added REF**: NPTH, NPTH, F.Cu at (101.3, 52.0)
- added REF**: NPTH, NPTH, F.Cu at (101.3, 113.0)
- added REF**: NPTH, NPTH, F.Cu at (50.0, 56.8)
- added REF**: NPTH, NPTH, F.Cu at (68.7, 67.0)
- added REF**: NPTH, NPTH, F.Cu at (33.7, 98.0)
- added REF**: NPTH, NPTH, F.Cu at (108.0, 43.0)
- added REF**: NPTH, NPTH, F.Cu at (107.0, 43.0)
- added REF**: NPTH, NPTH, F.Cu at (106.0, 121.0)
- added REF**: NPTH, NPTH, F.Cu at (101.3, 112.0)
- added REF**: NPTH, NPTH, F.Cu at (86.0, 43.2)
- added REF**: NPTH, NPTH, F.Cu at (85.0, 75.2)
- added REF**: NPTH, NPTH, F.Cu at (48.0, 43.2)
- added REF**: NPTH, NPTH, F.Cu at (33.5, 124.5)
- added REF**: NPTH, NPTH, F.Cu at (87.0, 91.2)
- added REF**: NPTH, NPTH, F.Cu at (85.0, 56.8)
- added REF**: NPTH, NPTH, F.Cu at (68.7, 114.0)
- added REF**: NPTH, NPTH, F.Cu at (49.0, 72.8)
- added REF**: NPTH, NPTH, F.Cu at (83.0, 107.2)
- added REF**: NPTH, NPTH, F.Cu at (52.0, 107.2)
- added REF**: NPTH, NPTH, F.Cu at (101.3, 49.0)
- added REF**: NPTH, NPTH, F.Cu at (33.7, 84.0)
- added REF**: NPTH, NPTH, F.Cu at (101.5, 40.5)
- added REF**: NPTH, NPTH, F.Cu at (68.7, 49.0)
- added REF**: NPTH, NPTH, F.Cu at (87.0, 75.2)
- added REF**: NPTH, NPTH, F.Cu at (86.0, 107.2)
- added REF**: NPTH, NPTH, F.Cu at (83.0, 88.8)
- added REF**: NPTH, NPTH, F.Cu at (87.0, 59.2)
- added REF**: NPTH, NPTH, F.Cu at (101.5, 127.5)
- added REF**: NPTH, NPTH, F.Cu at (83.0, 59.2)
- added REF**: NPTH, NPTH, F.Cu at (33.7, 49.0)
- added REF**: NPTH, NPTH, F.Cu at (85.0, 91.2)
- added REF**: NPTH, NPTH, F.Cu at (84.0, 56.8)
- added REF**: NPTH, NPTH, F.Cu at (49.0, 88.8)
- added REF**: NPTH, NPTH, F.Cu at (101.5, 123.5)
- added REF**: NPTH, NPTH, F.Cu at (51.0, 43.2)
- added REF**: NPTH, NPTH, F.Cu at (66.3, 116.0)
- added REF**: NPTH, NPTH, F.Cu at (101.3, 83.0)
- added REF**: NPTH, NPTH, F.Cu at (101.3, 50.0)
- added REF**: NPTH, NPTH, F.Cu at (66.3, 112.0)
- added REF**: NPTH, NPTH, F.Cu at (66.3, 81.0)
- added REF**: NPTH, NPTH, F.Cu at (68.7, 82.0)
- added REF**: NPTH, NPTH, F.Cu at (66.3, 100.0)
- added REF**: NPTH, NPTH, F.Cu at (50.0, 72.8)
- added REF**: NPTH, NPTH, F.Cu at (86.0, 72.8)
- added REF**: NPTH, NPTH, F.Cu at (49.0, 59.2)
- added REF**: NPTH, NPTH, F.Cu at (84.0, 104.8)
- added REF**: NPTH, NPTH, F.Cu at (33.7, 116.0)
- added REF**: NPTH, NPTH, F.Cu at (66.3, 64.0)
- added REF**: NPTH, NPTH, F.Cu at (51.0, 88.8)
- added REF**: NPTH, NPTH, F.Cu at (51.0, 75.2)
- added REF**: NPTH, NPTH, F.Cu at (66.3, 50.0)
- added REF**: NPTH, NPTH, F.Cu at (101.3, 65.0)
- added REF**: NPTH, NPTH, F.Cu at (87.0, 88.8)
- added REF**: NPTH, NPTH, F.Cu at (85.0, 120.8)
- added REF**: NPTH, NPTH, F.Cu at (66.3, 65.0)
- added REF**: NPTH, NPTH, F.Cu at (50.0, 120.8)
- added REF**: NPTH, NPTH, F.Cu at (51.0, 56.8)
- added REF**: NPTH, NPTH, F.Cu at (30.0, 43.0)
- added REF**: NPTH, NPTH, F.Cu at (68.7, 80.0)
- added REF**: NPTH, NPTH, F.Cu at (31.0, 43.0)
- added REF**: NPTH, NPTH, F.Cu at (106.0, 38.5)
- added REF**: NPTH, NPTH, F.Cu at (52.0, 59.2)
- added REF**: NPTH, NPTH, F.Cu at (101.3, 66.0)
- added REF**: NPTH, NPTH, F.Cu at (85.0, 107.2)
- added REF**: NPTH, NPTH, F.Cu at (101.3, 48.0)
- added REF**: NPTH, NPTH, F.Cu at (101.3, 98.0)
- added REF**: NPTH, NPTH, F.Cu at (68.7, 81.0)
- added REF**: NPTH, NPTH, F.Cu at (66.3, 49.0)
- added REF**: NPTH, NPTH, F.Cu at (101.3, 81.0)
- added REF**: NPTH, NPTH, F.Cu at (49.0, 43.2)
- added REF**: NPTH, NPTH, F.Cu at (33.7, 81.0)
- added REF**: NPTH, NPTH, F.Cu at (84.0, 107.2)
- added REF**: NPTH, NPTH, F.Cu at (86.0, 88.8)
- added REF**: NPTH, NPTH, F.Cu at (52.0, 104.8)
- added REF**: NPTH, NPTH, F.Cu at (68.7, 66.0)
- added REF**: NPTH, NPTH, F.Cu at (66.3, 67.0)
- added REF**: NPTH, NPTH, F.Cu at (85.0, 43.2)
- added REF**: NPTH, NPTH, F.Cu at (33.7, 83.0)
- added REF**: NPTH, NPTH, F.Cu at (83.0, 43.2)
- added REF**: NPTH, NPTH, F.Cu at (83.0, 91.2)
- added REF**: NPTH, NPTH, F.Cu at (68.7, 65.0)
- added REF**: NPTH, NPTH, F.Cu at (50.0, 59.2)
- added REF**: NPTH, NPTH, F.Cu at (48.0, 91.2)
- added REF**: NPTH, NPTH, F.Cu at (101.3, 68.0)
- added REF**: NPTH, NPTH, F.Cu at (66.3, 80.0)
- added REF**: NPTH, NPTH, F.Cu at (101.5, 38.5)
- added REF**: NPTH, NPTH, F.Cu at (33.7, 48.0)
- added REF**: NPTH, NPTH, F.Cu at (30.0, 121.0)
- added REF**: NPTH, NPTH, F.Cu at (51.0, 59.2)
- added REF**: NPTH, NPTH, F.Cu at (33.7, 115.0)
- added REF**: NPTH, NPTH, F.Cu at (104.0, 43.0)
- added REF**: NPTH, NPTH, F.Cu at (87.0, 107.2)
- added REF**: NPTH, NPTH, F.Cu at (33.7, 67.0)
- added REF**: NPTH, NPTH, F.Cu at (106.0, 43.0)
- added REF**: NPTH, NPTH, F.Cu at (87.0, 104.8)
- added REF**: NPTH, NPTH, F.Cu at (50.0, 91.2)
- added REF**: NPTH, NPTH, F.Cu at (68.7, 48.0)
- added REF**: NPTH, NPTH, F.Cu at (31.0, 121.0)
- added REF**: NPTH, NPTH, F.Cu at (66.3, 99.0)
- added REF**: NPTH, NPTH, F.Cu at (33.7, 64.0)
- added REF**: NPTH, NPTH, F.Cu at (85.0, 59.2)
- added REF**: NPTH, NPTH, F.Cu at (104.0, 121.0)
- added REF**: NPTH, NPTH, F.Cu at (66.3, 83.0)
- added REF**: NPTH, NPTH, F.Cu at (68.7, 97.0)
- added REF**: NPTH, NPTH, F.Cu at (48.0, 72.8)
- added REF**: NPTH, NPTH, F.Cu at (33.5, 37.5)
- added REF**: NPTH, NPTH, F.Cu at (101.3, 115.0)
- added REF**: NPTH, NPTH, F.Cu at (28.0, 121.0)
- added REF**: NPTH, NPTH, F.Cu at (68.7, 113.0)
- added REF**: NPTH, NPTH, F.Cu at (66.3, 98.0)
- added REF**: NPTH, NPTH, F.Cu at (108.0, 121.0)
- added REF**: NPTH, NPTH, F.Cu at (101.5, 126.5)
- added REF**: NPTH, NPTH, F.Cu at (66.3, 113.0)
- added REF**: NPTH, NPTH, F.Cu at (52.0, 75.2)
- added REF**: NPTH, NPTH, F.Cu at (48.0, 88.8)
- added REF**: NPTH, NPTH, F.Cu at (33.7, 99.0)
- added REF**: NPTH, NPTH, F.Cu at (52.0, 72.8)
- added REF**: NPTH, NPTH, F.Cu at (83.0, 120.8)
- added REF**: NPTH, NPTH, F.Cu at (66.3, 96.0)
- added REF**: NPTH, NPTH, F.Cu at (66.3, 68.0)
- added REF**: NPTH, NPTH, F.Cu at (84.0, 59.2)
- added REF**: NPTH, NPTH, F.Cu at (33.5, 123.5)
- added REF**: NPTH, NPTH, F.Cu at (68.7, 84.0)
- added REF**: Fiducial, Fiducial, F.Cu at (31.5, 125.5)
- added REF**: NPTH, NPTH, F.Cu at (86.0, 104.8)
- added REF**: Fiducial, Fiducial, F.Cu at (103.5, 38.5)
- added REF**: NPTH, NPTH, F.Cu at (52.0, 91.2)
- added REF**: NPTH, NPTH, F.Cu at (33.7, 65.0)
- added REF**: NPTH, NPTH, F.Cu at (84.0, 88.8)
- added REF**: NPTH, NPTH, F.Cu at (101.3, 97.0)
- added REF**: NPTH, NPTH, F.Cu at (101.3, 64.0)
- added REF**: NPTH, NPTH, F.Cu at (68.7, 100.0)
- added REF**: NPTH, NPTH, F.Cu at (83.0, 56.8)
- added REF**: NPTH, NPTH, F.Cu at (48.0, 104.8)
- added REF**: NPTH, NPTH, F.Cu at (84.0, 43.2)
- added REF**: NPTH, NPTH, F.Cu at (101.3, 80.0)
- added REF**: NPTH, NPTH, F.Cu at (33.5, 40.5)
- added REF**: NPTH, NPTH, F.Cu at (66.3, 51.0)
- added REF**: NPTH, NPTH, F.Cu at (87.0, 56.8)
- added REF**: NPTH, NPTH, F.Cu at (86.0, 59.2)
- added REF**: NPTH, NPTH, F.Cu at (68.7, 83.0)
- added REF**: NPTH, NPTH, F.Cu at (105.0, 121.0)
- added REF**: NPTH, NPTH, F.Cu at (101.3, 96.0)
- added REF**: NPTH, NPTH, F.Cu at (66.3, 97.0)
- added REF**: NPTH, NPTH, F.Cu at (29.0, 38.5)
- added REF**: NPTH, NPTH, F.Cu at (86.0, 56.8)
- added REF**: NPTH, NPTH, F.Cu at (68.7, 96.0)
- added REF**: NPTH, NPTH, F.Cu at (52.0, 56.8)
- added REF**: NPTH, NPTH, F.Cu at (33.7, 68.0)
- added REF**: NPTH, NPTH, F.Cu at (83.0, 75.2)
- added REF**: NPTH, NPTH, F.Cu at (52.0, 120.8)
- added REF**: NPTH, NPTH, F.Cu at (50.0, 104.8)
- added REF**: NPTH, NPTH, F.Cu at (66.3, 114.0)
- added REF**: NPTH, NPTH, F.Cu at (66.3, 48.0)
- added REF**: NPTH, NPTH, F.Cu at (101.3, 114.0)
- added REF**: NPTH, NPTH, F.Cu at (49.0, 56.8)
- added REF**: NPTH, NPTH, F.Cu at (101.5, 36.5)
- added REF**: Fiducial, Fiducial, B.Cu at (103.5, 38.5)
- added REF**: Fiducial, Fiducial, B.Cu at (31.5, 38.5)
- added REF**: Fiducial, Fiducial, B.Cu at (31.5, 125.5)
- added REF**: NPTH, NPTH, F.Cu at (85.0, 88.8)
- added REF**: NPTH, NPTH, F.Cu at (68.7, 52.0)
- added REF**: NPTH, NPTH, F.Cu at (52.0, 88.8)
- added REF**: NPTH, NPTH, F.Cu at (27.0, 43.0)
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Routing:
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- added copper zone on B.Cu, net Board_0-GND
- added copper zone on F.Cu, net Board_0-GND
- added copper zone on B.Cu, net Board_1-GND
- added copper zone on F.Cu, net Board_1-GND
- added copper zone on B.Cu, net Board_2-GND
- added copper zone on F.Cu, net Board_2-GND
- added copper zone on B.Cu, net Board_3-GND
- added copper zone on F.Cu, net Board_3-GND
- added copper zone on B.Cu, net Board_4-GND
- added copper zone on F.Cu, net Board_4-GND
- added copper zone on B.Cu, net Board_5-GND
- added copper zone on F.Cu, net Board_5-GND
- added copper zone on B.Cu, net Board_6-GND
- added copper zone on F.Cu, net Board_6-GND
- added copper zone on B.Cu, net Board_7-GND
- added copper zone on F.Cu, net Board_7-GND
- added copper zone on B.Cu, net Board_8-GND
- added copper zone on F.Cu, net Board_8-GND
- added copper zone on B.Cu, net Board_9-GND
- added copper zone on F.Cu, net Board_9-GND
- removed copper zone on B.Cu, net GND
- removed copper zone on F.Cu, net GND
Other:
- board size 70 x 84 mm -> 82 x 92 mm
- net class Default removed
- net class POWER removed
- rule pad_to_mask_clearance: 0.051 -> 0
- board text removed: "V-GROOVE"
